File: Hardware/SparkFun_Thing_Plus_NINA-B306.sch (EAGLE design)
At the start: 82 parts, among them J1 USB-C, J2 THING_PLUS_LOGICAL, J3 CONN_03X2, J4 MICRO-SDFRICTION, J6 QWIIC_RA, Q1 20V/4.2A/52mΩ/1.4W, Q2 220mA/50V/3.5Ω, Q3 20V/4.2A/52mΩ/1.4W, U1 ESD Diode, U2 U-BLOX_NINA_B306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

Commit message: Routing, end of week commit.
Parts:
- J3: value CONN_03X2 -> CONN_03X2_NO4; device MISC:CONN_03X2 -> MISC:CONN_03X2_NO4
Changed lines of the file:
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@@
 <setting verticaltext="up"/>
 </settings>
-<grid distance="0.1" unitdist="inch" unit="inch" style="lines" multiple="1" display="no" altdistance="0.01" altunitdist="inch" altunit="inch"/>
+<grid distance="0.1" unitdist="inch" unit="inch" style="lines" multiple="1" display="yes" altdistance="0.01" altunitdist="inch" altunit="inch"/>
 <layers>
 <layer number="1" name="Top" color="4" fill="1" visible="no" active="no"/>
@@
 <clearance class="4" value="0.15"/>
 </class>
-<class number="5" name="usb_diff" width="0.24" drill="0.3">
+<class number="5" name="usb_diff" width="0.2" drill="0.2">
 <clearance class="0" value="0.2"/>
-<clearance class="1" value="0.23"/>
-<clearance class="2" value="0.4"/>
+<clearance class="1" value="0.2"/>
+<clearance class="2" value="0.2"/>
 <clearance class="3" value="0.2"/>
 <clearance class="4" value="0.4"/>
-<clearance class="5" value="0.23"/>
+<clearance class="5" value="0.15"/>
 </class>
 </classes>
@@
 <part name="SUPPLY17" library="SparkFun-PowerSymbols" deviceset="3.3V" device=""/>
 <part name="GND15" library="SparkFun-PowerSymbols" deviceset="GND" device=""/>
-<part name="J3" library="MISC" deviceset="CONN_03X2" device=""/>
+<part name="J3" library="MISC" deviceset="CONN_03X2_NO4" device=""/>
 <part name="GND19" library="SparkFun-PowerSymbols" deviceset="GND" device=""/>
 <part name="GND23" library="SparkFun-PowerSymbols" deviceset="GND" device=""/>
@@
 <pinref part="U6" gate="G$1" pin="INT1"/>
 <wire x1="411.48" y1="149.86" x2="408.94" y2="149.86" width="0.1524" layer="91"/>
-<label x="411.48" y="149.86" size="1.27" layer="95" xref="yes"/>
+<label x="411.48" y="149.86" size="1.27" layer="95" font="vector" xref="yes"/>
 <pinref part="TP8" gate="G$1" pin="1"/>
 <wire x1="408.94" y1="149.86" x2="401.32" y2="149.86" width="0.1524" layer="91"/>
@@
 <pinref part="U2" gate="G$1" pin="IO21"/>
 <wire x1="109.22" y1="134.62" x2="106.68" y2="134.62" width="0.1524" layer="91"/>
-<label x="109.22" y="134.62" size="1.27" layer="95" xref="yes"/>
+<label x="109.22" y="134.62" size="1.27" layer="95" font="vector" xref="yes"/>
 </segment>
 </net>
@@
 <pinref part="U6" gate="G$1" pin="INT2"/>
 <wire x1="401.32" y1="147.32" x2="408.94" y2="147.32" width="0.1524" layer="91"/>
-<label x="411.48" y="147.32" size="1.27" layer="95" xref="yes"/>
+<label x="411.48" y="147.32" size="1.27" layer="95" font="vector" xref="yes"/>
 <pinref part="TP9" gate="G$1" pin="1"/>
 <wire x1="408.94" y1="147.32" x2="411.48" y2="147.32" width="0.1524" layer="91"/>
@@
 <pinref part="U2" gate="G$1" pin="IO22"/>
 <wire x1="109.22" y1="132.08" x2="106.68" y2="132.08" width="0.1524" layer="91"/>
-<label x="109.22" y="132.08" size="1.27" layer="95" xref="yes"/>
+<label x="109.22" y="132.08" size="1.27" layer="95" font="vector" xref="yes"/>
 </segment>
 </net>
@@
 <pinref part="U2" gate="G$1" pin="IO37"/>
 <wire x1="109.22" y1="111.76" x2="106.68" y2="111.76" width="0.1524" layer="91"/>
-<label x="109.22" y="111.76" size="1.27" layer="95" xref="yes"/>
+<label x="109.22" y="111.76" size="1.27" layer="95" font="vector" xref="yes"/>
 </segment>
 <segment>
 <wire x1="269.24" y1="22.86" x2="274.32" y2="22.86" width="0.1524" layer="91"/>
-<label x="269.24" y="22.86" size="1.27" layer="95" rot="MR0" xref="yes"/>
+<label x="269.24" y="22.86" size="1.27" layer="95" font="vector" rot="MR0" xref="yes"/>
 <pinref part="J4" gate="J1" pin="DET"/>
 <pinref part="TP4" gate="G$1" pin="1"/>

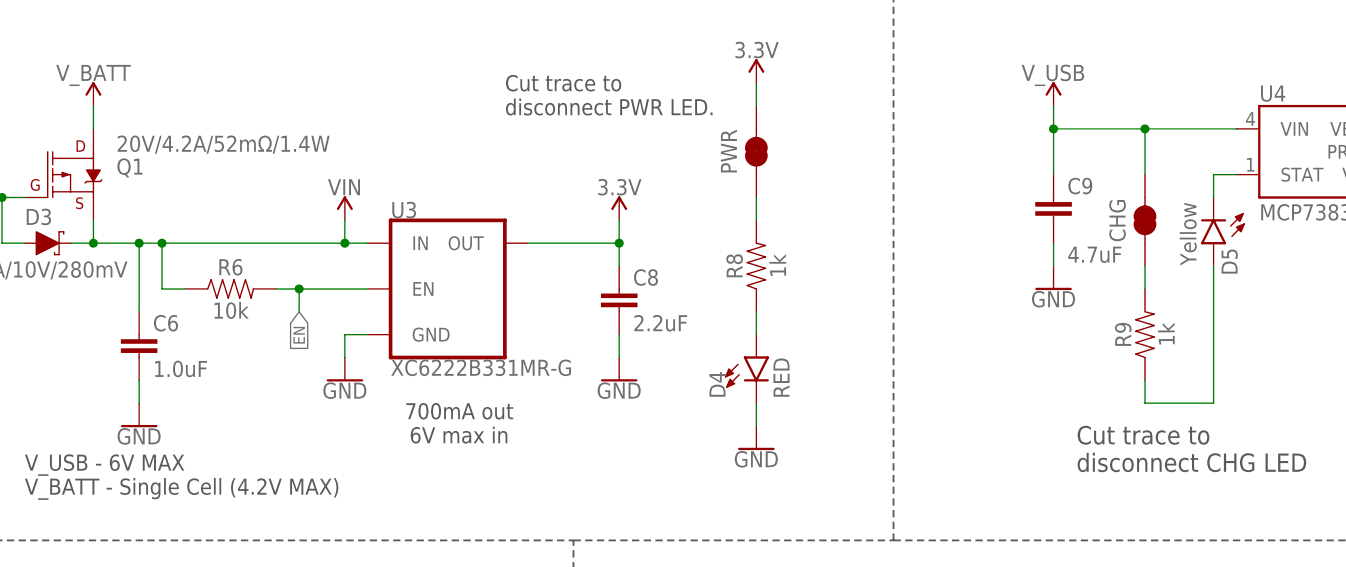
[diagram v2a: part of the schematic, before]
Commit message: routed and ready for v01 design review.
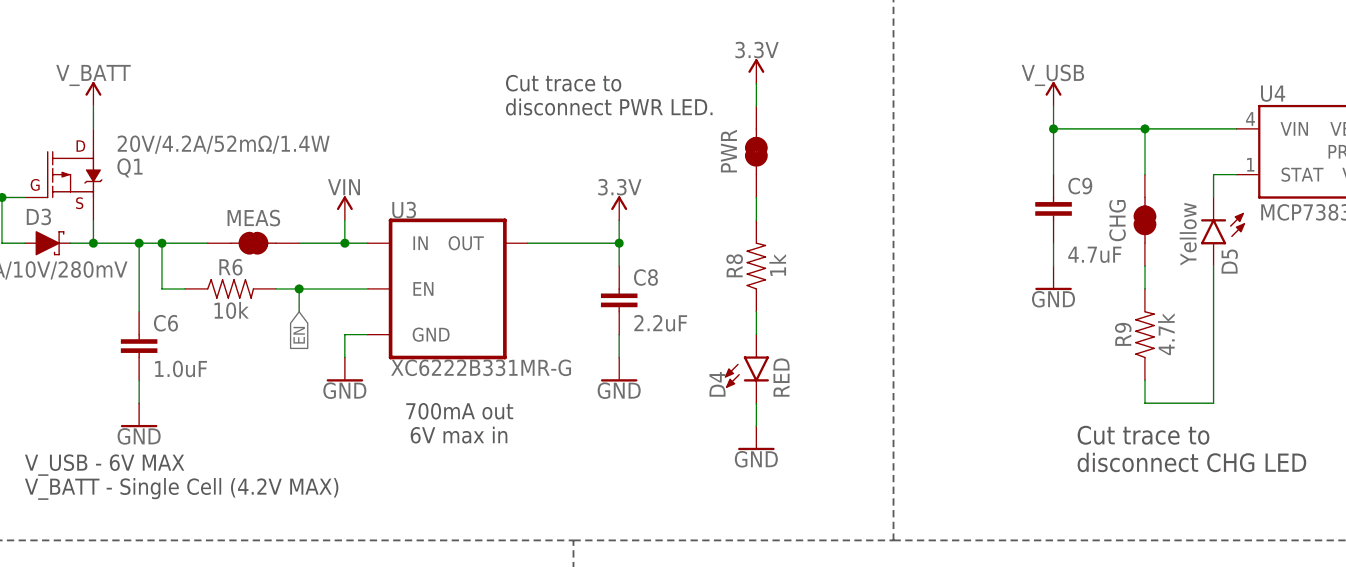
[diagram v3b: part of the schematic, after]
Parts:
- added MEAS: JUMPER-COMBO_2_NC_TRACE, SparkFun-Jumpers:JUMPER-COMBO_2_NC_TRACE
- R9: value 1k -> 4.7k; device SparkFun-Resistors:1KOHM-0402T-1/16W-1% -> SparkFun-Resistors:4.7KOHM-0402T-1/16W-1%
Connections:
- net N$1 renamed SHLD
- new net N$1: C6.1, D3.C, MEAS.1, Q1.S, R6.1
- net VIN: now also MEAS.2; no longer C6.1, D3.C, Q1.S, R6.1
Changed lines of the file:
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@@
 <setting verticaltext="up"/>
 </settings>
-<grid distance="0.1" unitdist="inch" unit="inch" style="lines" multiple="1" display="yes" altdistance="0.01" altunitdist="inch" altunit="inch"/>
+<grid distance="0.1" unitdist="inch" unit="inch" style="lines" multiple="1" display="no" altdistance="0.01" altunitdist="inch" altunit="inch"/>
 <layers>
 <layer number="1" name="Top" color="4" fill="1" visible="no" active="no"/>
@@
 </class>
 <class number="1" name="power" width="0.2" drill="0.3">
-<clearance class="1" value="0.2"/>
+<clearance class="1" value="0.18"/>
 </class>
 <class number="2" name="ground" width="0.11" drill="0.3">
@@
 <part name="U4" library="SparkFun-IC-Power" deviceset="MCP73831" device=""/>
 <part name="D5" library="SparkFun-LED" deviceset="LED-YELLOW" device="0603" value="Yellow"/>
-<part name="R9" library="SparkFun-Resistors" deviceset="1KOHM" device="-0402T-1/16W-1%" value="1k"/>
+<part name="R9" library="SparkFun-Resistors" deviceset="4.7KOHM" device="-0402T-1/16W-1%" value="4.7k"/>
 <part name="C9" library="SparkFun-Capacitors" deviceset="4.7UF" device="-0402_TIGHT-6.3V-20%-X5R" value="4.7uF"/>
 <part name="GND28" library="SparkFun-PowerSymbols" deviceset="GND" device=""/>
@@
 <part name="TP1" library="SparkFun-Connectors" deviceset="TEST-POINT" device="3X5" value="TEST-POINT3X5"/>
 <part name="TP6" library="SparkFun-Connectors" deviceset="TEST-POINT" device="3X5" value="TEST-POINT3X5"/>
+<part name="MEAS" library="SparkFun-Jumpers" deviceset="JUMPER-COMBO_2_NC_TRACE" device=""/>
 </parts>
 <sheets>
@@
 <instance part="LOGO2" gate="G$1" x="393.7" y="23.368" smashed="yes"/>
 <instance part="U7" gate="U1" x="388.62" y="91.44" smashed="yes">
-<attribute name="NAME" x="378.46" y="99.314" size="1.778" layer="95"/>
-<attribute name="VALUE" x="378.46" y="81.026" size="1.778" layer="95" align="top-left"/>
+<attribute name="NAME" x="378.46" y="99.314" size="1.778" layer="95" font="vector"/>
+<attribute name="VALUE" x="378.46" y="81.026" size="1.778" layer="95" font="vector" align="top-left"/>
 </instance>
 <instance part="GND34" gate="1" x="373.38" y="78.74" smashed="yes">
@@
 <attribute name="NAME" x="302.26" y="144.78" size="1.778" layer="95" font="vector" rot="R270"/>
 <attribute name="VALUE" x="299.72" y="152.4" size="1.778" layer="96" font="vector" rot="R270" display="off"/>
+</instance>
+<instance part="MEAS" gate="JP1" x="139.7" y="236.22" smashed="yes">
+<attribute name="NAME" x="139.7" y="239.014" size="1.778" layer="95" font="vector" align="center"/>
+<attribute name="VALUE" x="139.7" y="233.426" size="1.778" layer="96" font="vector" align="center" display="off"/>
 </instance>
 </instances>
@@
 </segment>
 </net>
-<net name="N$1" class="0">
+<net name="SHLD" class="2">
 <segment>
 <pinref part="J1" gate="J1" pin="SHLD"/>
@@
 <net name="VIN" class="1">
 <segment>
-<pinref part="D3" gate="G$1" pin="C"/>
 <pinref part="U3" gate="G$1" pin="IN"/>
-<wire x1="119.38" y1="236.22" x2="121.92" y2="236.22" width="0.1524" layer="91"/>
-<pinref part="Q1" gate="G$1" pin="S"/>
-<wire x1="121.92" y1="236.22" x2="127" y2="236.22" width="0.1524" layer="91"/>
-<wire x1="127" y1="236.22" x2="129.54" y2="236.22" width="0.1524" layer="91"/>
-<wire x1="129.54" y1="236.22" x2="149.86" y2="236.22" width="0.1524" layer="91"/>
 <wire x1="149.86" y1="236.22" x2="152.4" y2="236.22" width="0.1524" layer="91"/>
-<wire x1="121.92" y1="238.76" x2="121.92" y2="236.22" width="0.1524" layer="91"/>
-<junction x="121.92" y="236.22"/>
 <pinref part="SUPPLY5" gate="G$1" pin="VIN"/>
 <wire x1="149.86" y1="238.76" x2="149.86" y2="236.22" width="0.1524" layer="91"/>
+<pinref part="MEAS" gate="JP1" pin="2"/>
+<wire x1="144.78" y1="236.22" x2="149.86" y2="236.22" width="0.1524" layer="91"/>
 <junction x="149.86" y="236.22"/>
-<pinref part="R6" gate="G$1" pin="1"/>
-<wire x1="132.08" y1="231.14" x2="129.54" y2="231.14" width="0.1524" layer="91"/>
-<wire x1="129.54" y1="231.14" x2="129.54" y2="236.22" width="0.1524" layer="91"/>
-<junction x="129.54" y="236.22"/>
-<pinref part="C6" gate="G$1" pin="1"/>
-<wire x1="127" y1="228.6" x2="127" y2="236.22" width="0.1524" layer="91"/>
-<junction x="127" y="236.22"/>
 </segment>
 </net>
@@
 </segment>
 </net>
-<net name="SDA_PU_PWR" class="1">
+<net name="SDA_PU_PWR" class="0">
 <segment>
 <pinref part="R7" gate="G$1" pin="2"/>
@@
 </segment>
 </net>
-<net name="SCL_PU_PWR" class="1">
+<net name="SCL_PU_PWR" class="0">
 <segment>
 <pinref part="R5" gate="G$1" pin="2"/>
@@
 </segment>
 </net>
+<net name="N$1" class="1">
+<segment>
+<pinref part="D3" gate="G$1" pin="C"/>
+<wire x1="119.38" y1="236.22" x2="121.92" y2="236.22" width="0.1524" layer="91"/>
+<pinref part="Q1" gate="G$1" pin="S"/>
+<wire x1="121.92" y1="236.22" x2="127" y2="236.22" width="0.1524" layer="91"/>
+<wire x1="127" y1="236.22" x2="129.54" y2="236.22" width="0.1524" layer="91"/>
+<wire x1="121.92" y1="238.76" x2="121.92" y2="236.22" width="0.1524" layer="91"/>
+<junction x="121.92" y="236.22"/>
+<pinref part="R6" gate="G$1" pin="1"/>
+<wire x1="132.08" y1="231.14" x2="129.54" y2="231.14" width="0.1524" layer="91"/>
+<wire x1="129.54" y1="231.14" x2="129.54" y2="236.22" width="0.1524" layer="91"/>
+<pinref part="C6" gate="G$1" pin="1"/>
+<wire x1="127" y1="228.6" x2="127" y2="236.22" width="0.1524" layer="91"/>
+<junction x="127" y="236.22"/>
+<pinref part="MEAS" gate="JP1" pin="1"/>
+<wire x1="134.62" y1="236.22" x2="129.54" y2="236.22" width="0.1524" layer="91"/>
+<junction x="129.54" y="236.22"/>
+</segment>
+</net>

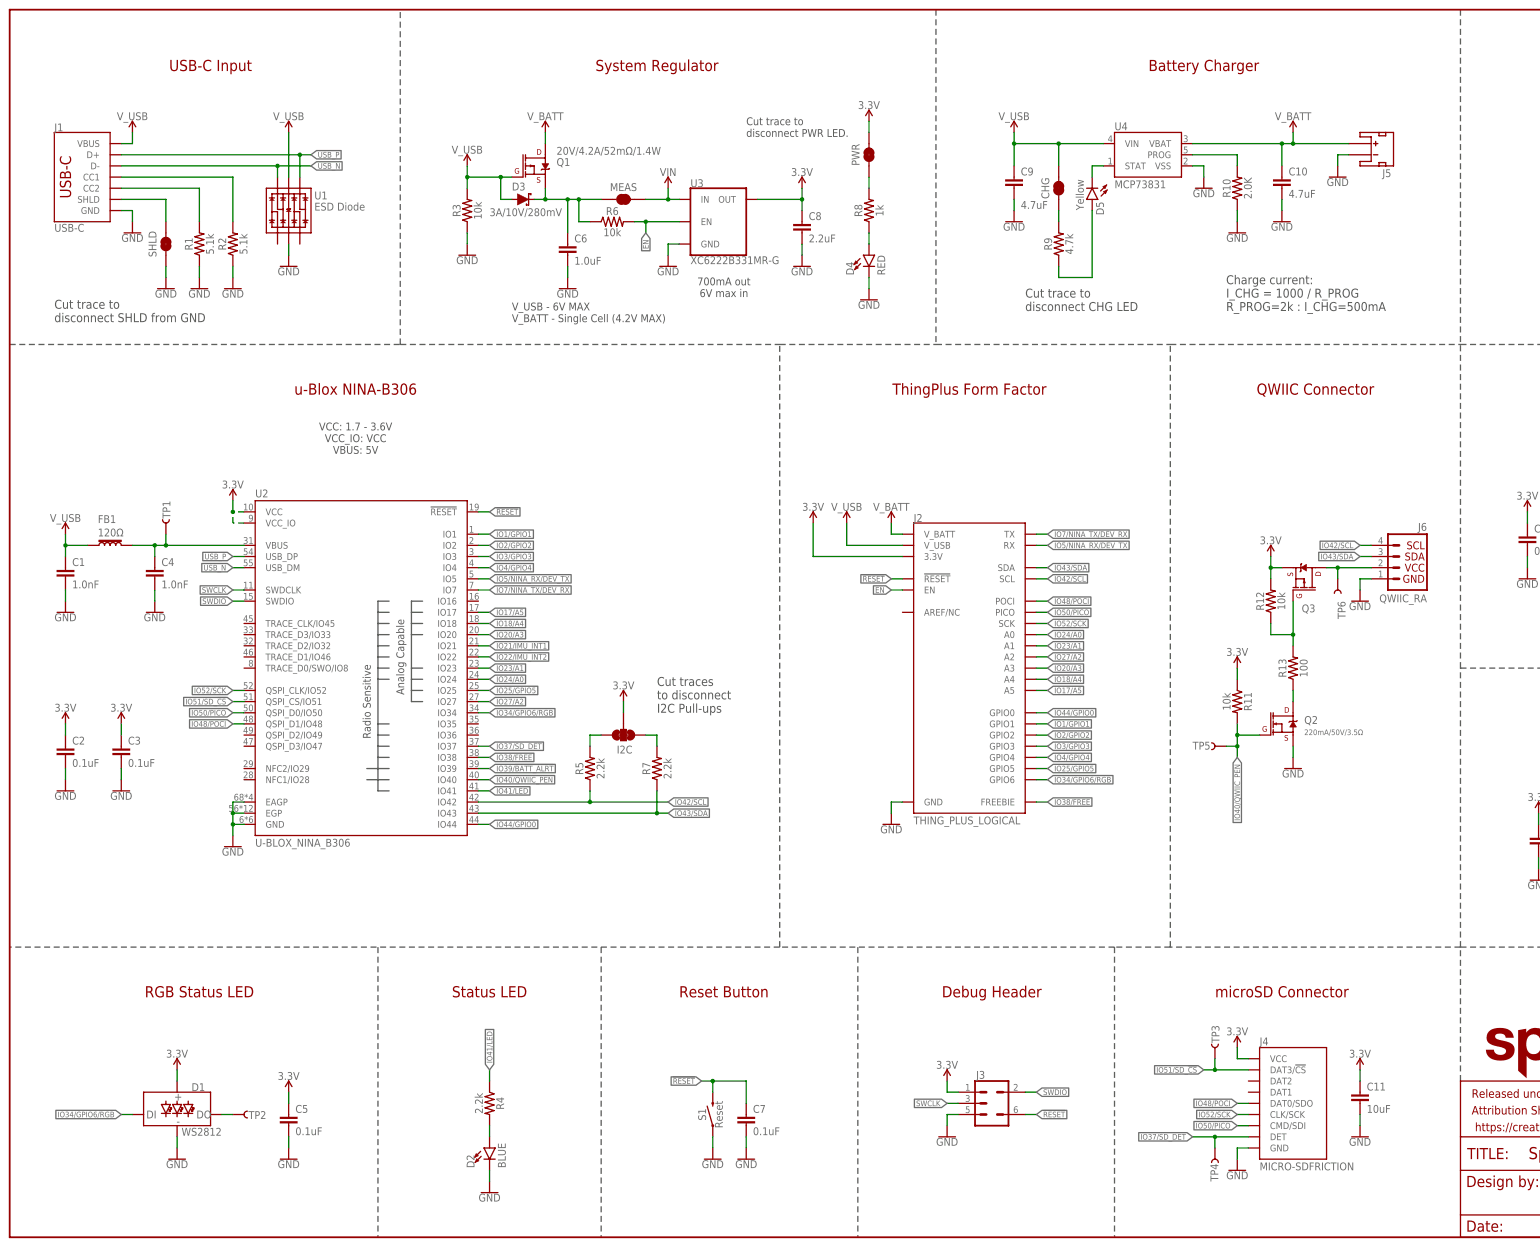
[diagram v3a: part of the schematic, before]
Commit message: v01 ready for production.
Move Power LED
Move MEAS jumper
Move GPIO6 to a new IO pin
Remove Q2
Allow ground pour between IO41 and SDA
Add vias next to BME280 ground pad
Shorten !RESET! top silk to !RST!
Swap CHG silk vertical direction
Add IMU silk from ISM BOB
Add more ground vias
Rotate !RST! on bottom silk
Reset button silk
LED silk
Add "NINA-B306" under module on top silk
Align LEDs vertically
Evenly space LEDs horizontally
Reroute
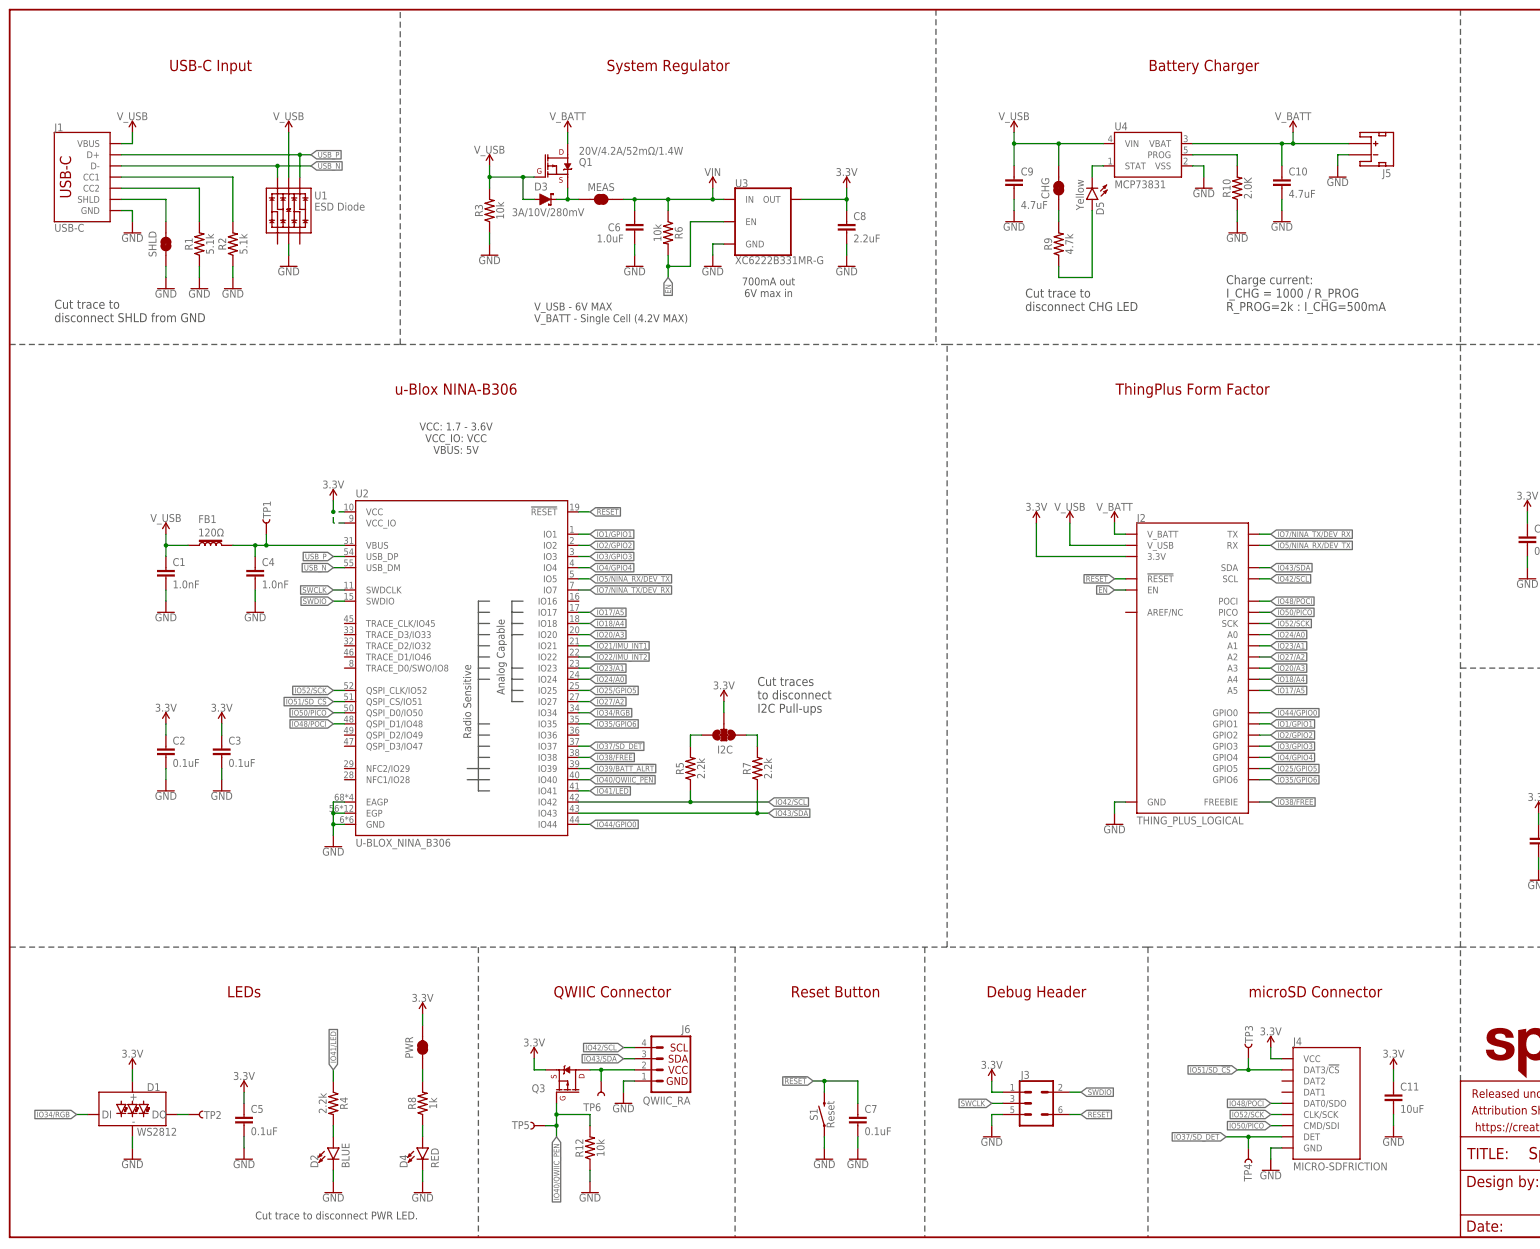
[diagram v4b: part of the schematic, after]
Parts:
- removed Q2: 220mA/50V/3.5Ω, SparkFun-DiscreteSemi:MOSFET-NCH-BSS138
- removed R11: 10k, SparkFun-Resistors:10KOHM-0402T-1/16W-1%
- removed R13: 100, SparkFun-Resistors:100OHM-0402-TIGHT-1/16W-1%
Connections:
- removed net IO34/GPIO6/RGB: D1.DI, J2.GPIO6, U2.IO34
- removed net IO40/QWIIC_PEN: Q2.G, R11.2, TP5.1, U2.IO40
- removed net N$1: C6.1, D3.C, MEAS.1, Q1.S, R6.1
- removed net N$13: Q2.D, R13.1
- removed net N$7: Q3.G, R12.1, R13.2
- new net IO34/RGB: D1.DI, U2.IO34
- new net IO35/GPIO6: J2.GPIO6, U2.IO35
- new net IO40/QWIIC_!PEN!: Q3.G, R12.2, TP5.1, U2.IO40
- new net N$12: D3.C, MEAS.1, Q1.S
- net 3.3V: no longer R11.1, R12.2
- net GND: now also R12.1; no longer Q2.S
- net VIN: now also C6.1, R6.1
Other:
- note added: "LEDs"
- note removed: "RGB Status LED"
- note removed: "Status LED"
- moved on the sheet: C1, C11, C2, C3, C4, C5, C6, C7, C8, D1, D2, D3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

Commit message: Update for v10 post-proto changes.
Add CHG LED silk
Flip silk text direction on rear !RST!
Change GPIO6/IO35 silk
Add silk for first pin on SWD pogo
Re-place updated ESD diode.
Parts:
- FRAME1: REV v01 -> v10
- U1: device SparkFun-DiscreteSemi:TVS_DIODE_ARRAYSMD -> SparkFun-DiscreteSemi:TVS_DIODE_ARRAY_DT1042-04SO-7
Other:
- moved on the sheet: C10, C6, C8, C9, CHG, D3, D5, J5, MEAS, Q1, R10, R3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
